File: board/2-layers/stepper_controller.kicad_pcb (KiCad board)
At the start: 4 copper layers, 126 parts, among them J201 USB_OTG, P101 JTAG, P102 JTAG, P103 CONN_4, P104 CONN_8X2, P105 CONN_4, P106 CONN_6X2, P107 CONN_4, P201 CONN_2X2, P301 12V_Conn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

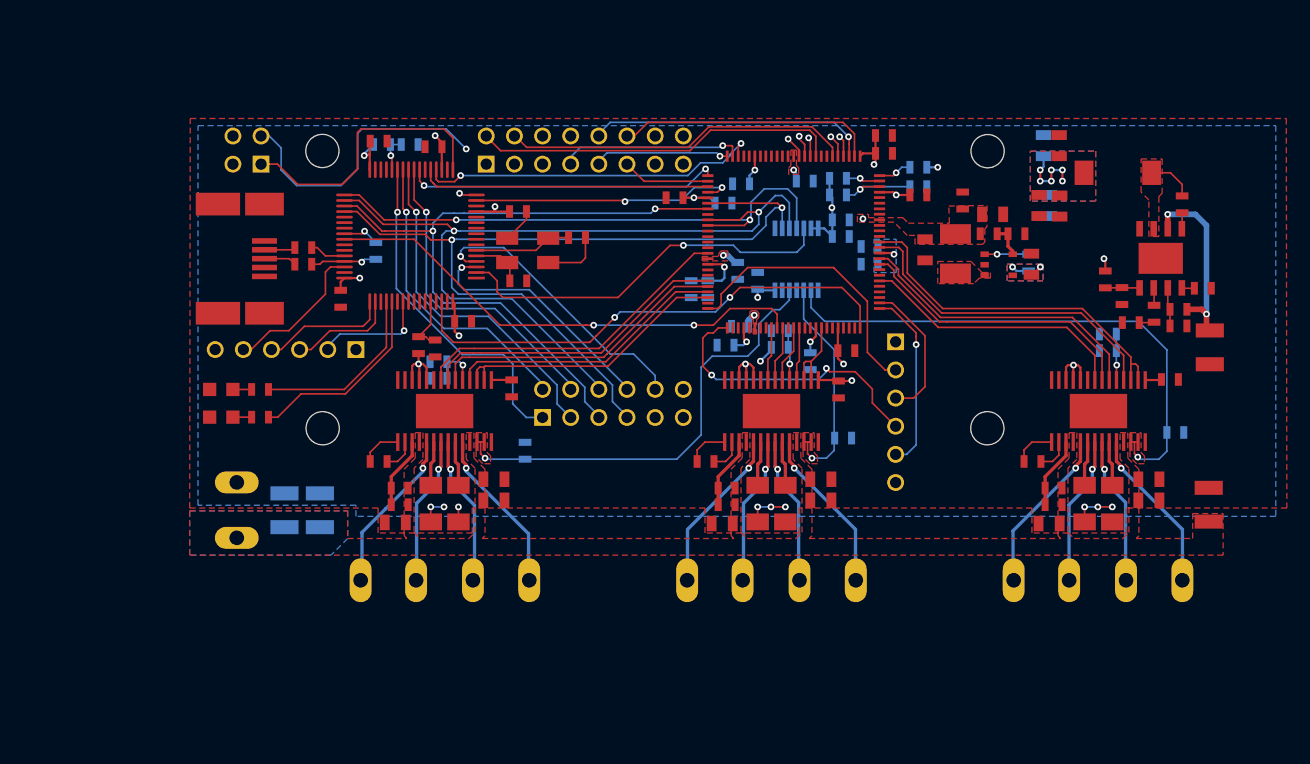
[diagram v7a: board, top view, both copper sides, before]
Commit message: added an other 7 point connector
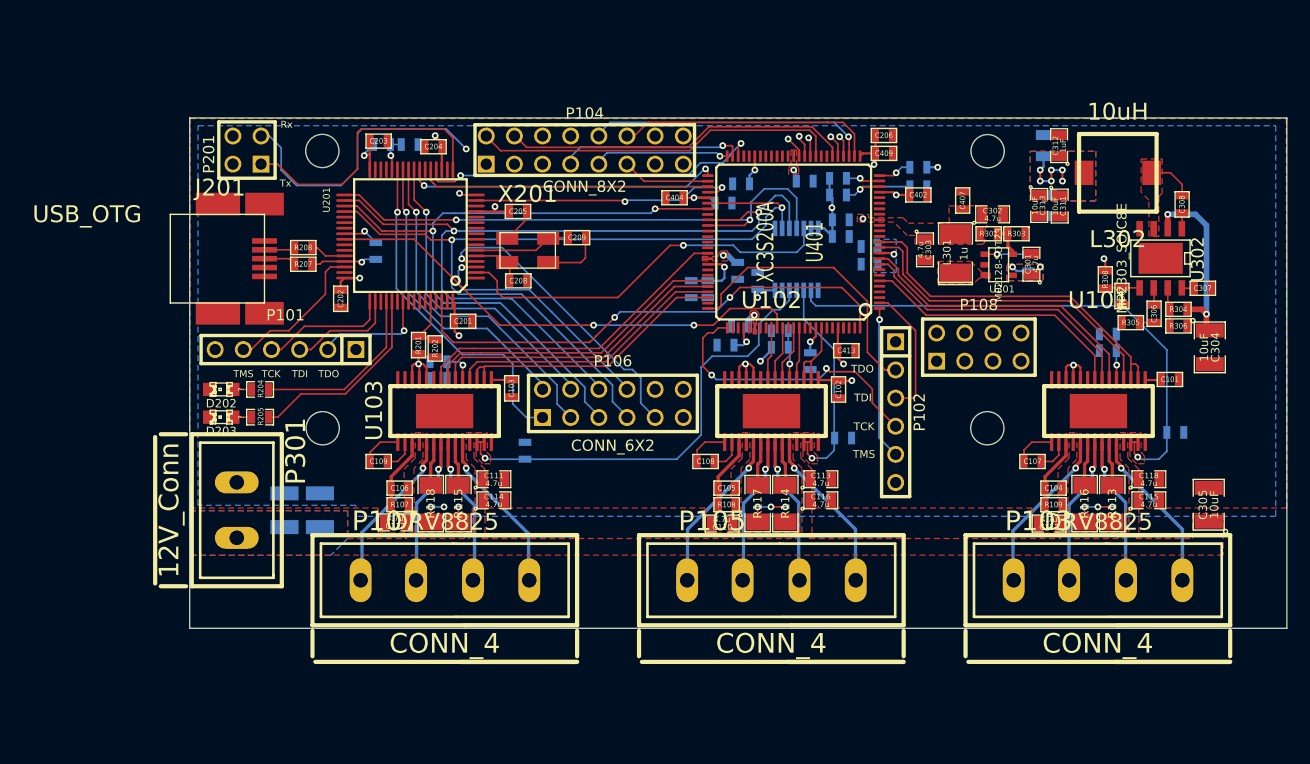
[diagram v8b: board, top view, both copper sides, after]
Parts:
- added P108: CONN_4X2, pin_array_4x2, F.Cu at (176.5, 107.0)
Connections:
- P106 pad 10: /STM32/PC15 -> +3.3V
- P106 pad 9: +3.3V -> /STM32/PC15
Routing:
- net FPGA_TMS: track 16.5 -> 13.8 mm
- net /STM32/PC15: track 25.8 -> 27.3 mm
- net FPGA_TDI: track 13.0 -> 12.1 mm
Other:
- board outline added: 99 x 46 mm
